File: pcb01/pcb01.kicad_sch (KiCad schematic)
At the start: 59 parts, among them J1 DIN41612_02x32_AC, J11 Conn_01x09, J2 Jmp_UART_Irq, J3 Conn_01x09_Socket, J4 Conn_01x08_Socket, J5 UART, J6 Conn_01x02_Socket, J7 Jmp_Irq, J8 Jmp_NMI, J9 Ram1 Enable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

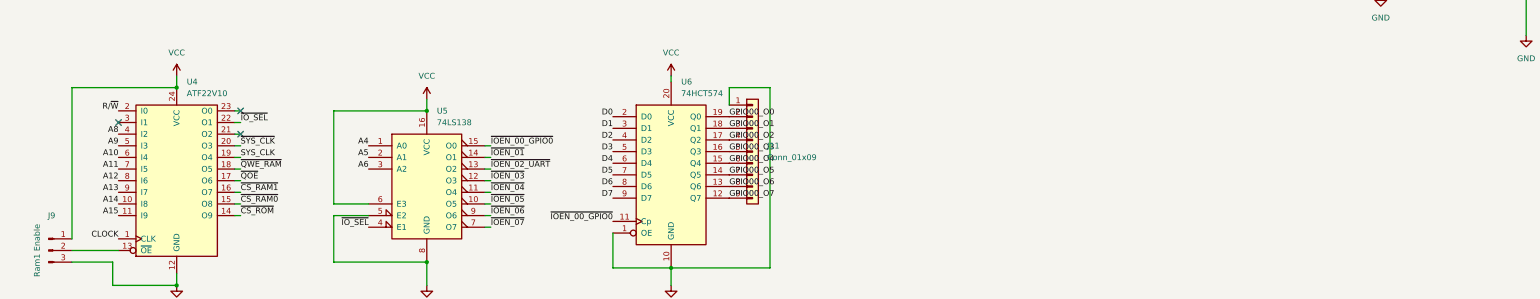
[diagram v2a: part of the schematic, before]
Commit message: big pld reorder & break out unused pins
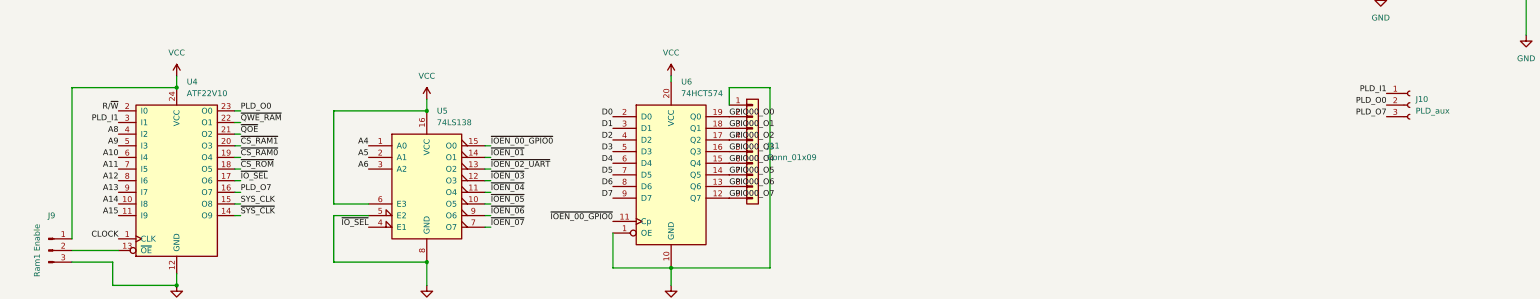
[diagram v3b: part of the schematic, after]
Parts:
- added J10: PLD_aux, Connector_PinSocket_2.54mm:PinSocket_1x03_P2.54mm_Vertical, symbol Connector:Conn_01x03_Socket
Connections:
- net SYS_CLK: now also U4.15 (O8); no longer U4.19 (O4)
- net ~{CS_RAM0}: now also U4.19 (O4); no longer U4.15 (O8)
- net ~{CS_RAM1}: now also U4.20 (O3); no longer U4.16 (O7)
- net ~{CS_ROM}: now also U4.18 (O5); no longer U4.14 (O9)
- net ~{IO_SEL}: now also U4.17 (O6); no longer U4.22 (O1)
- net ~{QOE}: now also U4.21 (O2); no longer U4.17 (O6)
- net ~{QWE_RAM}: now also U4.22 (O1); no longer U4.18 (O5)
- net ~{SYS_CLK}: now also U4.14 (O9); no longer U4.20 (O3)
- net PLD_O0: now reaches U4.23 (O0)
- net PLD_O0: now also J10.2 (Pin_2)
- net PLD_I1: now reaches U4.3 (I1)
- net PLD_I1: now also J10.1 (Pin_1)
- new net PLD_O7: J10.3 (Pin_3), U4.16 (O7)
- no-connect marks 35 -> 32
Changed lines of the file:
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@@
   (no_connect (at 396.24 222.25))
   (no_connect (at 396.24 201.93))
-  (no_connect (at 62.23 236.22))
   (no_connect (at 325.12 198.12))
   (no_connect (at 382.27 217.17))
@@
   (no_connect (at 396.24 237.49))
   (no_connect (at 396.24 204.47))
-  (no_connect (at 35.56 238.76))
-  (no_connect (at 62.23 241.3))
   (no_connect (at 396.24 227.33))
   (no_connect (at 142.24 33.02))
@@
     (effects (font (size 1.27 1.27)) (justify right bottom))
   )
+  (label "PLD_O0" (at 312.42 234.95 180) (fields_autoplaced)
+    (effects (font (size 1.27 1.27)) (justify right bottom))
+  )
   (label "A13" (at 383.54 176.53 180) (fields_autoplaced)
     (effects (font (size 1.27 1.27)) (justify right bottom))
@@
     (effects (font (size 1.27 1.27)) (justify right bottom))
   )
-  (label "~{QWE_RAM}" (at 62.23 248.92 0) (fields_autoplaced)
-    (effects (font (size 1.27 1.27)) (justify left bottom))
-  )
   (label "A13" (at 228.6 162.56 180) (fields_autoplaced)
     (effects (font (size 1.27 1.27)) (justify right bottom))
@@
     (effects (font (size 1.27 1.27)) (justify right bottom))
   )
+  (label "~{IO_SEL}" (at 62.23 251.46 0) (fields_autoplaced)
+    (effects (font (size 1.27 1.27)) (justify left bottom))
+  )
   (label "UART_IP1" (at 292.1 162.56 180) (fields_autoplaced)
     (effects (font (size 1.27 1.27)) (justify right bottom))
@@
     (effects (font (size 1.27 1.27)) (justify left bottom))
   )
+  (label "~{QOE}" (at 62.23 241.3 0) (fields_autoplaced)
+    (effects (font (size 1.27 1.27)) (justify left bottom))
+  )
   (label "~{CS_ROM}" (at 389.89 138.43 0) (fields_autoplaced)
     (effects (font (size 1.27 1.27)) (justify left bottom))
   )
-  (label "~{CS_ROM}" (at 62.23 259.08 0) (fields_autoplaced)
-    (effects (font (size 1.27 1.27)) (justify left bottom))
-  )
   (label "UART_IP2" (at 354.33 205.74 180) (fields_autoplaced)
     (effects (font (size 1.27 1.27)) (justify right bottom))
@@
     (effects (font (size 1.27 1.27)) (justify right bottom))
   )
-  (label "~{QOE}" (at 62.23 251.46 0) (fields_autoplaced)
-    (effects (font (size 1.27 1.27)) (justify left bottom))
-  )
   (label "UART_IP1" (at 354.33 203.2 180) (fields_autoplaced)
     (effects (font (size 1.27 1.27)) (justify right bottom))
@@
     (effects (font (size 1.27 1.27)) (justify right bottom))
   )
+  (label "PLD_I1" (at 35.56 238.76 180) (fields_autoplaced)
+    (effects (font (size 1.27 1.27)) (justify right bottom))
+  )
   (label "UART_IP6" (at 354.33 215.9 180) (fields_autoplaced)
     (effects (font (size 1.27 1.27)) (justify right bottom))
@@
     (effects (font (size 1.27 1.27)) (justify right bottom))
   )
+  (label "~{CS_RAM0}" (at 62.23 246.38 0) (fields_autoplaced)
+    (effects (font (size 1.27 1.27)) (justify left bottom))
+  )
   (label "UART_IP4" (at 354.33 210.82 180) (fields_autoplaced)
     (effects (font (size 1.27 1.27)) (justify right bottom))
   )
-  (label "~{CS_RAM0}" (at 62.23 256.54 0) (fields_autoplaced)
-    (effects (font (size 1.27 1.27)) (justify left bottom))
-  )
   (label "A11" (at 134.62 163.83 180) (fields_autoplaced)
     (effects (font (size 1.27 1.27)) (justify right bottom))
@@
     (effects (font (size 1.27 1.27)) (justify right bottom))
   )
+  (label "~{QWE_RAM}" (at 62.23 238.76 0) (fields_autoplaced)
+    (effects (font (size 1.27 1.27)) (justify left bottom))
+  )
   (label "~{IOEN_01}" (at 116.84 246.38 0) (fields_autoplaced)
     (effects (font (size 1.27 1.27)) (justify left bottom))
@@
     (effects (font (size 1.27 1.27)) (justify right bottom))
   )
+  (label "~{CS_RAM1}" (at 62.23 243.84 0) (fields_autoplaced)
+    (effects (font (size 1.27 1.27)) (justify left bottom))
+  )
   (label "A14" (at 228.6 165.1 180) (fields_autoplaced)
     (effects (font (size 1.27 1.27)) (justify right bottom))
@@
     (effects (font (size 1.27 1.27)) (justify right bottom))
   )
+  (label "SYS_CLK" (at 62.23 256.54 0) (fields_autoplaced)
+    (effects (font (size 1.27 1.27)) (justify left bottom))
+  )
   (label "D6" (at 325.12 190.5 0) (fields_autoplaced)
     (effects (font (size 1.27 1.27)) (justify left bottom))
@@
     (effects (font (size 1.27 1.27)) (justify left bottom))
   )
-  (label "SYS_CLK" (at 62.23 246.38 0) (fields_autoplaced)
-    (effects (font (size 1.27 1.27)) (justify left bottom))
-  )
   (label "RX_D1" (at 292.1 187.96 180) (fields_autoplaced)
     (effects (font (size 1.27 1.27)) (justify right bottom))
@@
     (effects (font (size 1.27 1.27)) (justify left bottom))
   )
-  (label "~{SYS_CLK}" (at 62.23 243.84 0) (fields_autoplaced)
-    (effects (font (size 1.27 1.27)) (justify left bottom))
-  )
   (label "D7" (at 143.51 255.27 180) (fields_autoplaced)
     (effects (font (size 1.27 1.27)) (justify right bottom))
@@
     (effects (font (size 1.27 1.27)) (justify left bottom))
   )
+  (label "PLD_I1" (at 312.42 232.41 180) (fields_autoplaced)
+    (effects (font (size 1.27 1.27)) (justify right bottom))
+  )
   (label "A1" (at 383.54 207.01 180) (fields_autoplaced)
     (effects (font (size 1.27 1.27)) (justify right bottom))
@@
     (effects (font (size 1.27 1.27)) (justify right bottom))
   )
+  (label "PLD_O0" (at 62.23 236.22 0) (fields_autoplaced)
+    (effects (font (size 1.27 1.27)) (justify left bottom))
+  )
   (label "UART_OP3" (at 356.87 171.45 180) (fields_autoplaced)
     (effects (font (size 1.27 1.27)) (justify right bottom))
@@
     (effects (font (size 1.27 1.27)) (justify right bottom))
   )
+  (label "PLD_O7" (at 312.42 237.49 180) (fields_autoplaced)
+    (effects (font (size 1.27 1.27)) (justify right bottom))
+  )
   (label "A6" (at 134.62 151.13 180) (fields_autoplaced)
     (effects (font (size 1.27 1.27)) (justify right bottom))
@@
     (effects (font (size 1.27 1.27)) (justify left bottom))
   )
+  (label "~{SYS_CLK}" (at 62.23 259.08 0) (fields_autoplaced)
+    (effects (font (size 1.27 1.27)) (justify left bottom))
+  )
   (label "D2" (at 396.24 184.15 0) (fields_autoplaced)
     (effects (font (size 1.27 1.27)) (justify left bottom))
@@
     (effects (font (size 1.27 1.27)) (justify left bottom))
   )
+  (label "PLD_O7" (at 62.23 254 0) (fields_autoplaced)
+    (effects (font (size 1.27 1.27)) (justify left bottom))
+  )
   (label "A2" (at 134.62 140.97 180) (fields_autoplaced)
     (effects (font (size 1.27 1.27)) (justify right bottom))
@@
     (effects (font (size 1.27 1.27)) (justify right bottom))
   )
-  (label "~{CS_RAM1}" (at 62.23 254 0) (fields_autoplaced)
-    (effects (font (size 1.27 1.27)) (justify left bottom))
-  )
   (label "A4" (at 228.6 139.7 180) (fields_autoplaced)
     (effects (font (size 1.27 1.27)) (justify right bottom))
@@
     (effects (font (size 1.27 1.27)) (justify left bottom))
   )
+  (label "~{CS_ROM}" (at 62.23 248.92 0) (fields_autoplaced)
+    (effects (font (size 1.27 1.27)) (justify left bottom))
+  )
   (label "UART_OP2" (at 325.12 142.24 0) (fields_autoplaced)
     (effects (font (size 1.27 1.27)) (justify left bottom))
@@
   )
   (label "D7" (at 162.56 153.67 0) (fields_autoplaced)
-    (effects (font (size 1.27 1.27)) (justify left bottom))
-  )
-  (label "~{IO_SEL}" (at 62.23 238.76 0) (fields_autoplaced)
     (effects (font (size 1.27 1.27)) (justify left bottom))
   )
@@
         )
       )
+    )
+  )
+  (symbol (lib_id "Connector:Conn_01x03_Socket") (at 317.5 234.95 0) (unit 1)
+    (in_bom yes) (on_board yes) (dnp no) (fields_autoplaced)
+    (property "Reference" "J10" (at 318.77 233.68 0)
+      (effects (font (size 1.27 1.27)) (justify left))
+    )
+    (property "Value" "PLD_aux" (at 318.77 236.22 0)
+      (effects (font (size 1.27 1.27)) (justify left))
+    )
+    (property "Footprint" "Connector_PinSocket_2.54mm:PinSocket_1x03_P2.54mm_Vertical" (at 317.5 234.95 0)
+      (effects (font (size 1.27 1.27)) hide)
+    )
+    (property "Datasheet" "~" (at 317.5 234.95 0)
+      (effects (font (size 1.27 1.27)) hide)
+    )
+    (pin "1")
+    (pin "3")
+    (pin "2")
+    (instances
+      (project "pcb01"
+        (path "/a9a73dc6-7f92-4458-9da8-49621d12e480"
+          (reference "J10") (unit 1)
+        )
+      )

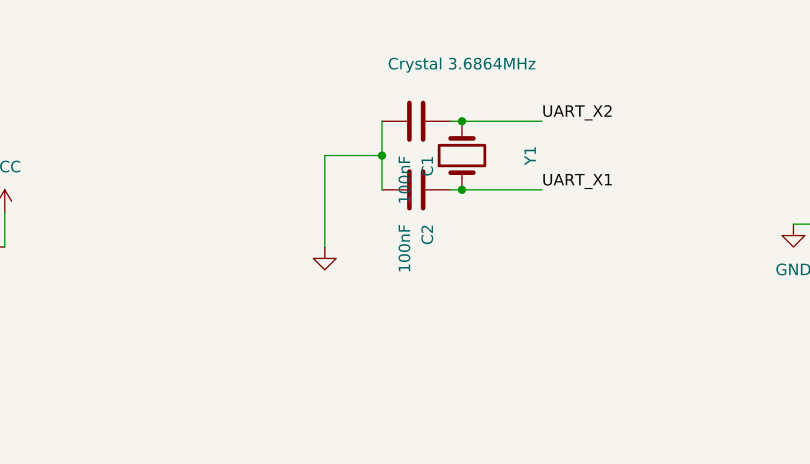
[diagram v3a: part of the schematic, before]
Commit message: mostly change resistors & caps to smd
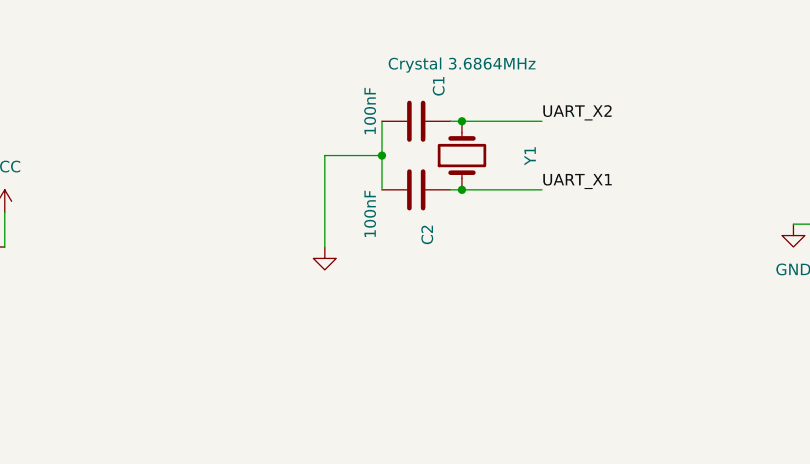
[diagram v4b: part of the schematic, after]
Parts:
- C10, C14, C3, C4, C5, C6, C7, C8, C9: footprint Capacitor_THT:C_Disc_D4.7mm_W2.5mm_P5.00mm -> Capacitor_SMD:C_0805_2012Metric_Pad1.18x1.45mm_HandSolder
- R1, R2, R3, R4: footprint Resistor_THT:R_Axial_DIN0207_L6.3mm_D2.5mm_P7.62mm_Horizontal -> Resistor_SMD:R_0805_2012Metric_Pad1.20x1.40mm_HandSolder
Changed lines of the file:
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@@
       (effects (font (size 1.27 1.27)) (justify left))
     )
-    (property "Footprint" "Capacitor_THT:C_Disc_D4.7mm_W2.5mm_P5.00mm" (at 341.3252 38.1 0)
+    (property "Footprint" "Capacitor_SMD:C_0805_2012Metric_Pad1.18x1.45mm_HandSolder" (at 341.3252 38.1 0)
       (effects (font (size 1.27 1.27)) hide)
     )
@@
       (effects (font (size 1.27 1.27)))
     )
-    (property "Footprint" "Resistor_THT:R_Axial_DIN0207_L6.3mm_D2.5mm_P7.62mm_Horizontal" (at 196.85 42.418 90)
+    (property "Footprint" "Resistor_SMD:R_0805_2012Metric_Pad1.20x1.40mm_HandSolder" (at 196.85 42.418 90)
       (effects (font (size 1.27 1.27)) hide)
     )
@@
       (effects (font (size 1.27 1.27)) (justify left))
     )
-    (property "Footprint" "Capacitor_THT:C_Disc_D4.7mm_W2.5mm_P5.00mm" (at 347.6752 38.1 0)
+    (property "Footprint" "Capacitor_SMD:C_0805_2012Metric_Pad1.18x1.45mm_HandSolder" (at 347.6752 38.1 0)
       (effects (font (size 1.27 1.27)) hide)
     )
@@
       (effects (font (size 1.27 1.27)) (justify left))
     )
-    (property "Footprint" "Capacitor_THT:C_Disc_D4.7mm_W2.5mm_P5.00mm" (at 310.8452 38.1 0)
+    (property "Footprint" "Capacitor_SMD:C_0805_2012Metric_Pad1.18x1.45mm_HandSolder" (at 310.8452 38.1 0)
       (effects (font (size 1.27 1.27)) hide)
     )
@@
       (effects (font (size 1.27 1.27)) (justify right))
     )
-    (property "Footprint" "Resistor_THT:R_Axial_DIN0207_L6.3mm_D2.5mm_P7.62mm_Horizontal" (at 347.218 135.89 90)
+    (property "Footprint" "Resistor_SMD:R_0805_2012Metric_Pad1.20x1.40mm_HandSolder" (at 347.218 135.89 90)
       (effects (font (size 1.27 1.27)) hide)
     )
@@
       (effects (font (size 1.27 1.27)) (justify left))
     )
-    (property "Footprint" "Capacitor_THT:C_Disc_D4.7mm_W2.5mm_P5.00mm" (at 334.9752 38.1 0)
+    (property "Footprint" "Capacitor_SMD:C_0805_2012Metric_Pad1.18x1.45mm_HandSolder" (at 334.9752 38.1 0)
       (effects (font (size 1.27 1.27)) hide)
     )
@@
       (effects (font (size 1.27 1.27)) (justify left))
     )
-    (property "Footprint" "Capacitor_THT:C_Disc_D4.7mm_W2.5mm_P5.00mm" (at 295.6052 38.1 0)
+    (property "Footprint" "Capacitor_SMD:C_0805_2012Metric_Pad1.18x1.45mm_HandSolder" (at 295.6052 38.1 0)
       (effects (font (size 1.27 1.27)) hide)
     )
@@
       (effects (font (size 1.27 1.27)) (justify right))
     )
-    (property "Footprint" "Capacitor_THT:C_Disc_D4.7mm_W2.5mm_P5.00mm" (at 354.0252 38.1 0)
+    (property "Footprint" "Capacitor_SMD:C_0805_2012Metric_Pad1.18x1.45mm_HandSolder" (at 354.0252 38.1 0)
       (effects (font (size 1.27 1.27)) hide)
     )
@@
       (effects (font (size 1.27 1.27)) (justify left))
     )
-    (property "Footprint" "Capacitor_THT:C_Disc_D4.7mm_W2.5mm_P5.00mm" (at 303.2252 38.1 0)
+    (property "Footprint" "Capacitor_SMD:C_0805_2012Metric_Pad1.18x1.45mm_HandSolder" (at 303.2252 38.1 0)
       (effects (font (size 1.27 1.27)) hide)
     )
@@
       (effects (font (size 1.27 1.27)))
     )
-    (property "Footprint" "Resistor_THT:R_Axial_DIN0207_L6.3mm_D2.5mm_P7.62mm_Horizontal" (at 124.46 27.178 90)
+    (property "Footprint" "Resistor_SMD:R_0805_2012Metric_Pad1.20x1.40mm_HandSolder" (at 124.46 27.178 90)
       (effects (font (size 1.27 1.27)) hide)
     )
@@
   )
   (symbol (lib_id "Device:C") (at 246.38 34.29 270) (unit 1)
-    (in_bom yes) (on_board yes) (dnp no) (fields_autoplaced)
+    (in_bom yes) (on_board yes) (dnp no)
     (property "Reference" "C2" (at 247.65 38.1 0)
       (effects (font (size 1.27 1.27)) (justify left))
     )
-    (property "Value" "100nF" (at 245.11 38.1 0)
+    (property "Value" "100nF" (at 241.3 34.29 0)
       (effects (font (size 1.27 1.27)) (justify left))
     )
@@
       (effects (font (size 1.27 1.27)) (justify left))
     )
-    (property "Footprint" "Capacitor_THT:C_Disc_D4.7mm_W2.5mm_P5.00mm" (at 318.4652 38.1 0)
+    (property "Footprint" "Capacitor_SMD:C_0805_2012Metric_Pad1.18x1.45mm_HandSolder" (at 318.4652 38.1 0)
       (effects (font (size 1.27 1.27)) hide)
     )
@@
   )
   (symbol (lib_id "Device:C") (at 246.38 26.67 270) (unit 1)
-    (in_bom yes) (on_board yes) (dnp no) (fields_autoplaced)
-    (property "Reference" "C1" (at 247.65 30.48 0)
-      (effects (font (size 1.27 1.27)) (justify left))
-    )
-    (property "Value" "100nF" (at 245.11 30.48 0)
+    (in_bom yes) (on_board yes) (dnp no)
+    (property "Reference" "C1" (at 248.92 21.59 0)
+      (effects (font (size 1.27 1.27)) (justify left))
+    )
+    (property "Value" "100nF" (at 241.3 22.86 0)
       (effects (font (size 1.27 1.27)) (justify left))
     )
@@
       (effects (font (size 1.27 1.27)) (justify left))
     )
-    (property "Footprint" "Capacitor_THT:C_Disc_D4.7mm_W2.5mm_P5.00mm" (at 327.3552 38.1 0)
+    (property "Footprint" "Capacitor_SMD:C_0805_2012Metric_Pad1.18x1.45mm_HandSolder" (at 327.3552 38.1 0)
       (effects (font (size 1.27 1.27)) hide)
     )
@@
       (effects (font (size 1.27 1.27)) (justify left))
     )
-    (property "Footprint" "Resistor_THT:R_Axial_DIN0207_L6.3mm_D2.5mm_P7.62mm_Horizontal" (at 173.482 27.94 90)
-      (effects (font (size 1.27 1.27)) hide)
-    )
+    (property "Footprint" "Resistor_SMD:R_0805_2012Metric_Pad1.20x1.40mm_HandSolder" (at 173.482 27.94 90)
+      (effects (font (size 1.27 1.27)) hide)
+    )

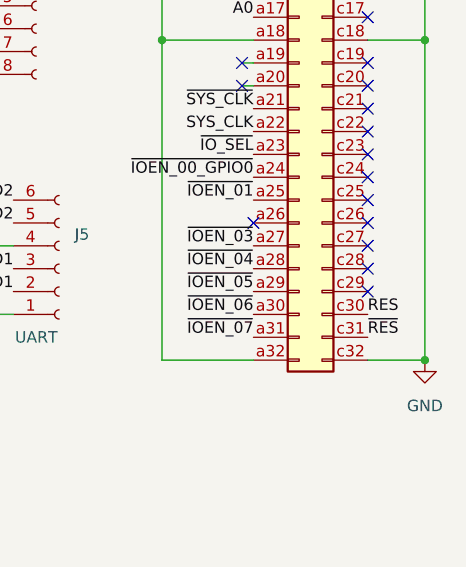
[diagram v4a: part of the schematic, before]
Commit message: connect rw to external connector
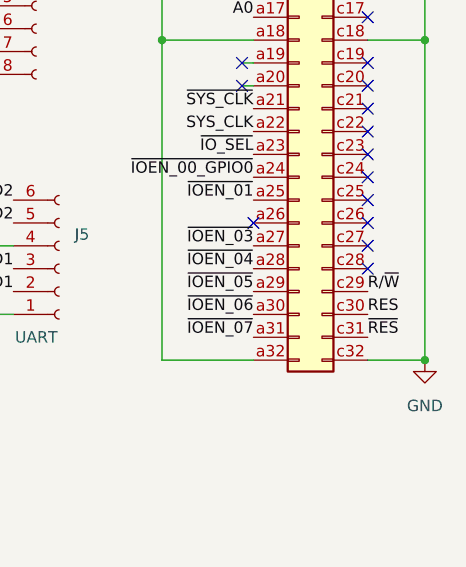
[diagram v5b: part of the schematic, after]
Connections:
- net R/~{W}: now also J1.c29 (Pin_c29)
- no-connect marks 32 -> 31
